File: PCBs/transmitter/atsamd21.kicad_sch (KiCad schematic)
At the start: 13 parts, among them U1 ATSAMD21G18A-A, Y1 32768Hz

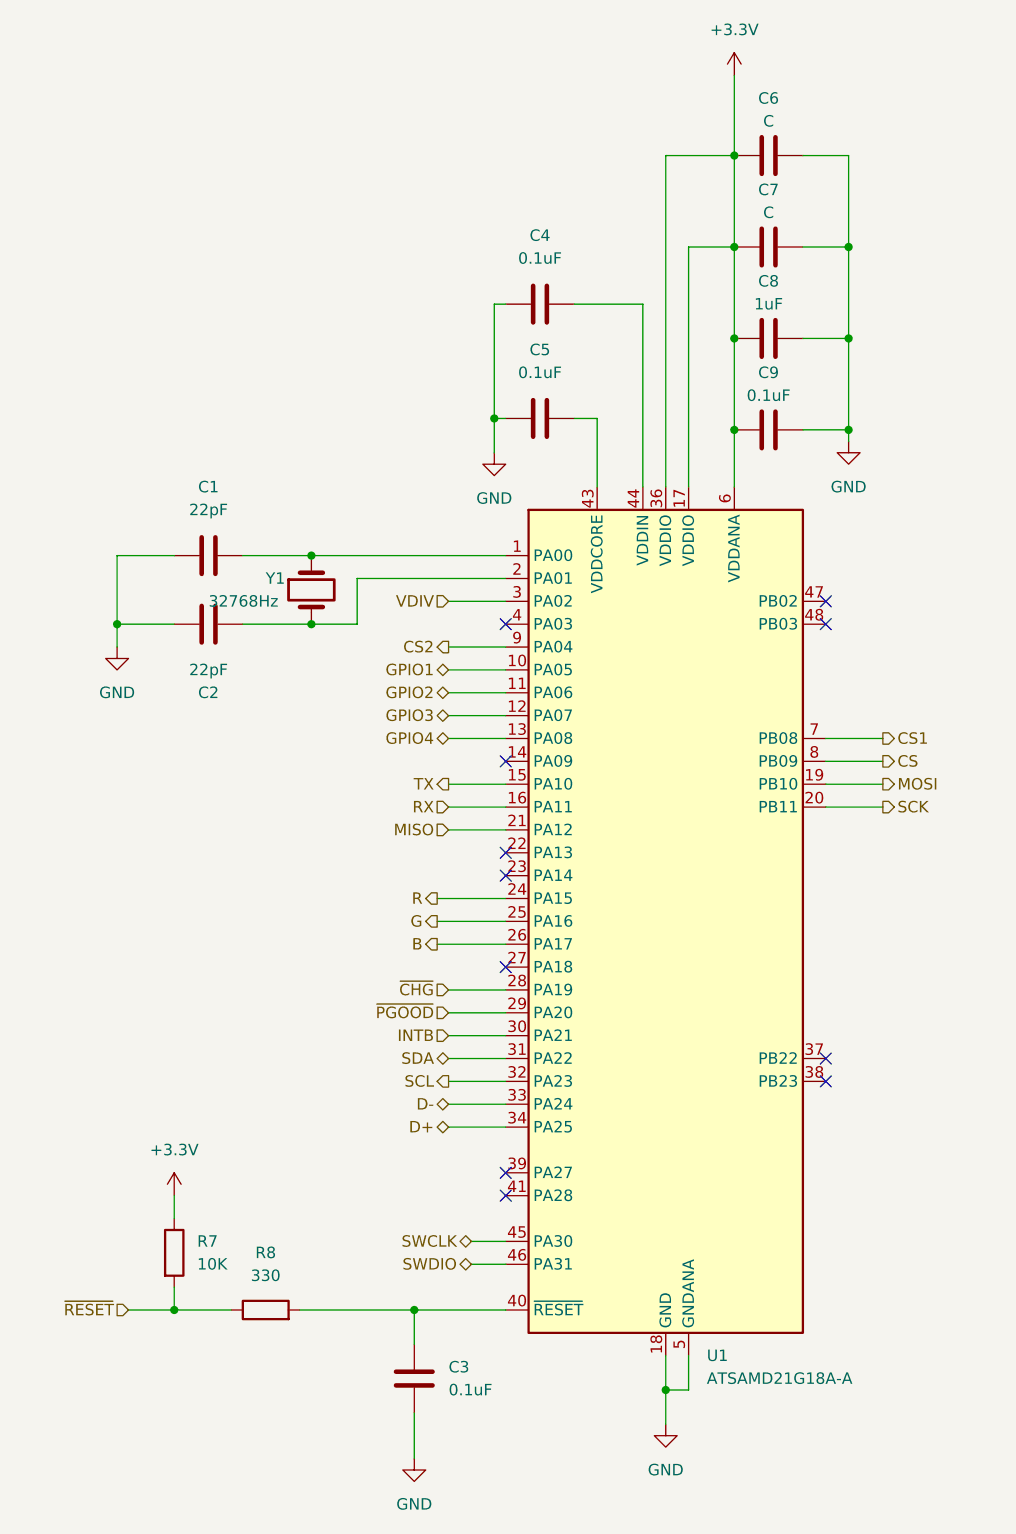
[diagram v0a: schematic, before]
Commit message: updated schematics
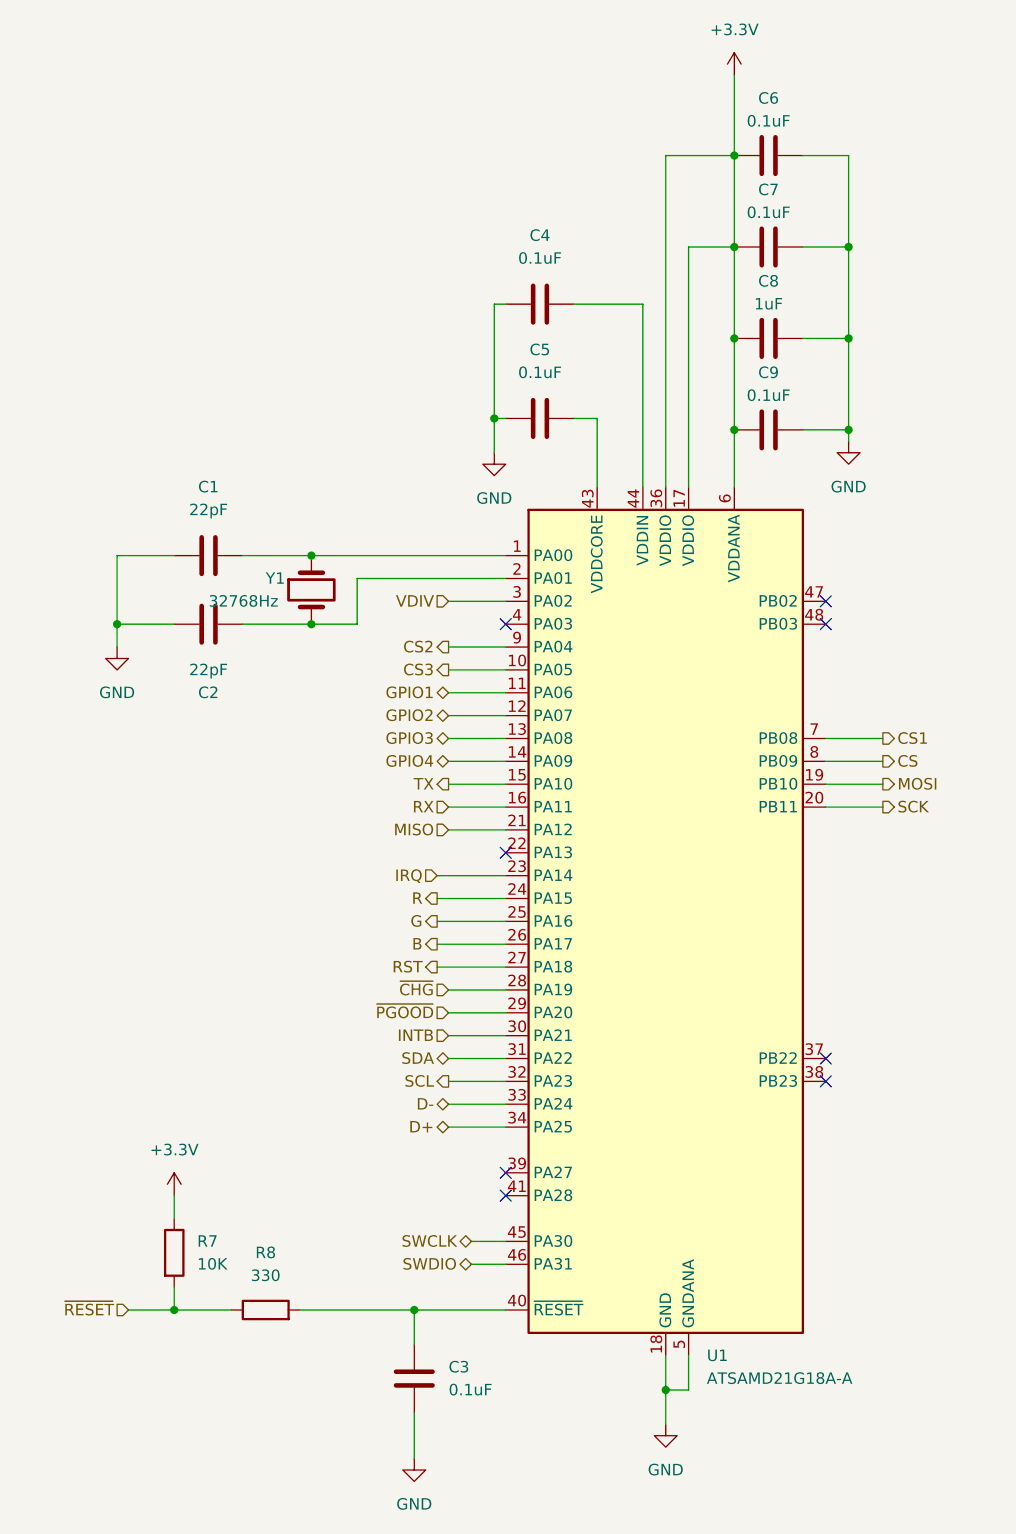
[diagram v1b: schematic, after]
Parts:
- C1, C2, C3, C4, C5, C8, C9: footprint (none) -> Capacitor_SMD:C_0603_1608Metric
- C6, C7: value C -> 0.1uF; footprint (none) -> Capacitor_SMD:C_0603_1608Metric
- R7, R8: footprint (none) -> Resistor_SMD:R_0603_1608Metric
- Y1: footprint (none) -> Crystal:XTAL_ABS07-32.768KHZ-T
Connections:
- net GPIO1: now also U1.11 (PA06); no longer U1.10 (PA05)
- net GPIO2: now also U1.12 (PA07); no longer U1.11 (PA06)
- net GPIO3: now also U1.13 (PA08); no longer U1.12 (PA07)
- net GPIO4: now also U1.14 (PA09); no longer U1.13 (PA08)
- net IRQ: now reaches U1.23 (PA14)
- net RST: now reaches U1.27 (PA18)
- new net CS3: U1.10 (PA05)
- no-connect marks 11 -> 8

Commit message: completed PCB layout
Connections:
- net CS2: now also U1.28 (PA19); no longer U1.9 (PA04)
- net CS3: now also U1.29 (PA20); no longer U1.10 (PA05)
- net ~{CHG}: now also U1.9 (PA04); no longer U1.28 (PA19)
- net ~{PGOOD}: now also U1.10 (PA05); no longer U1.29 (PA20)
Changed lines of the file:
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@@
+    (stroke (width 0) (type default) (color 0 0 0 0))
+  )
+  (wire (pts (xy 124.46 129.54) (xy 130.81 129.54))
     (stroke (width 0) (type default) (color 0 0 0 0))
   )
@@
     (stroke (width 0) (type default) (color 0 0 0 0))
   )
+  (wire (pts (xy 124.46 91.44) (xy 130.81 91.44))
+    (stroke (width 0) (type default) (color 0 0 0 0))
+  )
   (wire (pts (xy 166.37 106.68) (xy 172.72 106.68))
     (stroke (width 0) (type default) (color 0 0 0 0))
@@
     (stroke (width 0) (type default) (color 0 0 0 0))
   )
-  (wire (pts (xy 124.46 129.54) (xy 130.81 129.54))
-    (stroke (width 0) (type default) (color 0 0 0 0))
-  )
   (wire (pts (xy 124.46 134.62) (xy 130.81 134.62))
     (stroke (width 0) (type default) (color 0 0 0 0))
@@
     (stroke (width 0) (type default) (color 0 0 0 0))
   )
+  (wire (pts (xy 124.46 127) (xy 130.81 127))
+    (stroke (width 0) (type default) (color 0 0 0 0))
+  )
   (wire (pts (xy 163.83 64.77) (xy 168.91 64.77))
     (stroke (width 0) (type default) (color 0 0 0 0))
@@
     (stroke (width 0) (type default) (color 0 0 0 0))
   )
-  (wire (pts (xy 124.46 127) (xy 130.81 127))
-    (stroke (width 0) (type default) (color 0 0 0 0))
-  )
   (wire (pts (xy 140.97 63.5) (xy 140.97 71.12))
     (stroke (width 0) (type default) (color 0 0 0 0))
@@
     (stroke (width 0) (type default) (color 0 0 0 0))
   )
-  (wire (pts (xy 124.46 91.44) (xy 130.81 91.44))
-    (stroke (width 0) (type default) (color 0 0 0 0))
-  )
   (wire (pts (xy 163.83 44.45) (xy 168.91 44.45))
     (stroke (width 0) (type default) (color 0 0 0 0))
@@
     (stroke (width 0) (type default) (color 0 0 0 0))
   )
+  (wire (pts (xy 124.46 88.9) (xy 130.81 88.9))
+    (stroke (width 0) (type default) (color 0 0 0 0))
+  )
   (wire (pts (xy 156.21 34.29) (xy 156.21 44.45))
     (stroke (width 0) (type default) (color 0 0 0 0))
@@
     (stroke (width 0) (type default) (color 0 0 0 0))
   )
-  (wire (pts (xy 124.46 88.9) (xy 130.81 88.9))
-    (stroke (width 0) (type default) (color 0 0 0 0))
-  )
   (wire (pts (xy 148.59 71.12) (xy 148.59 34.29))
     (stroke (width 0) (type default) (color 0 0 0 0))
@@
     (stroke (width 0) (type default) (color 0 0 0 0))
   )
-  (hierarchical_label "~{CHG}" (shape input) (at 124.46 127 180)
+  (hierarchical_label "~{CHG}" (shape input) (at 124.46 88.9 180)
     (effects (font (size 1.27 1.27)) (justify right))
   )
@@
     (effects (font (size 1.27 1.27)) (justify right))
   )
-  (hierarchical_label "~{PGOOD}" (shape input) (at 124.46 129.54 180)
+  (hierarchical_label "~{PGOOD}" (shape input) (at 124.46 91.44 180)
     (effects (font (size 1.27 1.27)) (justify right))
   )
@@
     (effects (font (size 1.27 1.27)) (justify right))
   )
-  (hierarchical_label "CS2" (shape output) (at 124.46 88.9 180)
+  (hierarchical_label "CS2" (shape output) (at 124.46 127 180)
     (effects (font (size 1.27 1.27)) (justify right))
   )
@@
     (effects (font (size 1.27 1.27)) (justify right))
   )
-  (hierarchical_label "CS3" (shape output) (at 124.46 91.44 180)
-    (effects (font (size 1.27 1.27)) (justify right))
-  )
+  (hierarchical_label "CS3" (shape output) (at 124.46 129.54 180)
+    (effects (font (size 1.27 1.27)) (justify right))
+  )

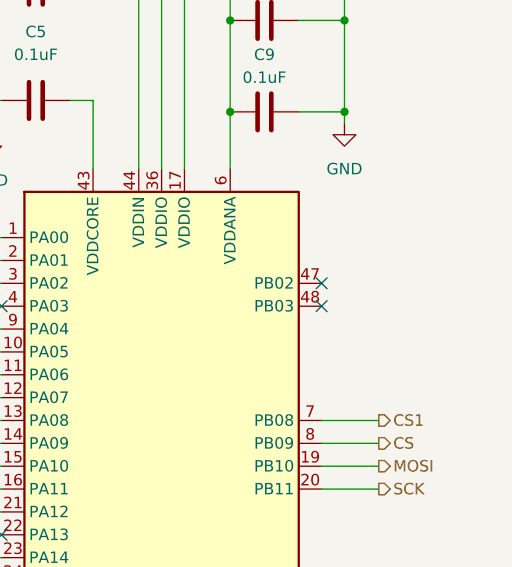
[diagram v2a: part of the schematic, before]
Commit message: created sensor board
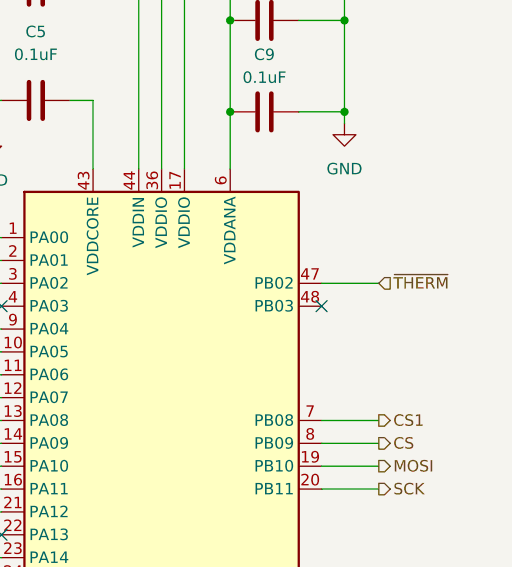
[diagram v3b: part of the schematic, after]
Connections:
- net ~{THERM}: now reaches U1.47 (PB02)
- no-connect marks 8 -> 7
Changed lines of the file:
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@@
   (no_connect (at 166.37 134.62))
   (no_connect (at 166.37 137.16))
-  (no_connect (at 166.37 83.82))
   (wire (pts (xy 138.43 63.5) (xy 140.97 63.5))
     (stroke (width 0) (type default) (color 0 0 0 0))
@@
     (stroke (width 0) (type default) (color 0 0 0 0))
   )
+  (wire (pts (xy 172.72 83.82) (xy 166.37 83.82))
+    (stroke (width 0) (type default) (color 0 0 0 0))
+  )
   (wire (pts (xy 123.19 119.38) (xy 130.81 119.38))
     (stroke (width 0) (type default) (color 0 0 0 0))
@@
     (effects (font (size 1.27 1.27)) (justify left))
   )
+  (hierarchical_label "~{THERM}" (shape input) (at 172.72 83.82 0)
+    (effects (font (size 1.27 1.27)) (justify left))
+  )
